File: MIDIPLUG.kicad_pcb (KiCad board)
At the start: 2 copper layers, 34 x 23.4 mm, 28 parts, among them J1 Wavetable Connector, U1 LP2985-3.3, U2 SAM2695, U3 4050, Y1 12Mhz

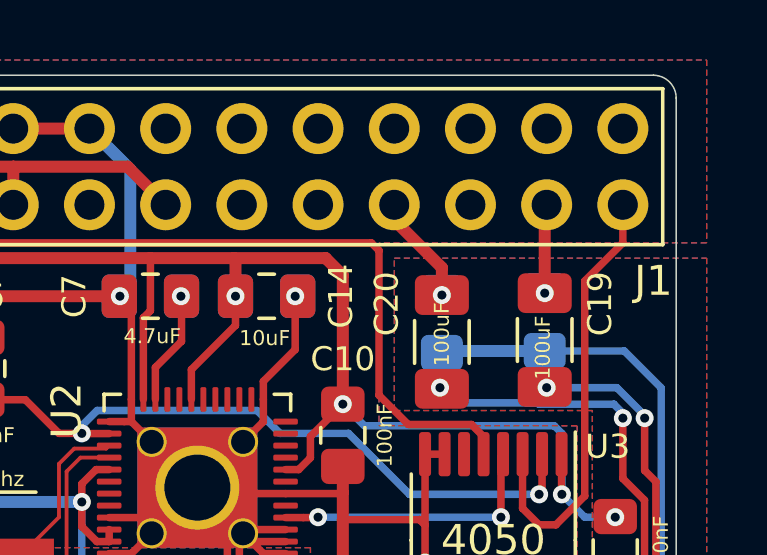
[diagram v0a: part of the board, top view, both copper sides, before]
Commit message: Connect GNDA
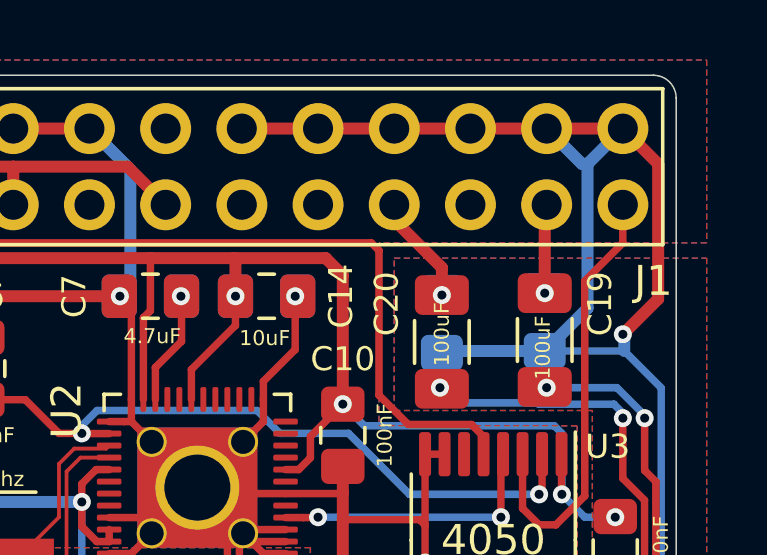
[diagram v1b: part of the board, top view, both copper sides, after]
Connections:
- J1 pad 15: (no net) -> GNDA
- J1 pad 17: (no net) -> GNDA
- J1 pad 19: (no net) -> GNDA
- J1 pad 21: (no net) -> GNDA
- J1 pad 23: (no net) -> GNDA
- J1 pad 25: (no net) -> GNDA
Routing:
- net GNDA: track 47.0 -> 78.4 mm, vias 2 -> 3
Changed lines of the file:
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@@
     (thickness 1.6)
     (drawings 13)
-    (tracks 331)
+    (tracks 348)
     (zones 0)
     (modules 28)
@@
   )
   (setup
-    (last_trace_width 0.127)
+    (last_trace_width 0.4)
     (user_trace_width 0.127)
     (user_trace_width 0.25)
@@
     (add_net "Net-(C6-Pad1)")
     (add_net "Net-(C7-Pad2)")
+    (add_net "Net-(J1-Pad12)")
+    (add_net "Net-(J1-Pad13)")
+    (add_net "Net-(J1-Pad16)")
+    (add_net "Net-(J1-Pad18)")
+    (add_net "Net-(J1-Pad2)")
+    (add_net "Net-(J1-Pad22)")
+    (add_net "Net-(J1-Pad8)")
     (add_net "Net-(U2-Pad16)")
+    (add_net "Net-(U2-Pad24)")
+    (add_net "Net-(U2-Pad26)")
+    (add_net "Net-(U2-Pad27)")
+    (add_net "Net-(U2-Pad28)")
+    (add_net "Net-(U2-Pad29)")
+    (add_net "Net-(U2-Pad3)")
+    (add_net "Net-(U2-Pad30)")
+    (add_net "Net-(U2-Pad32)")
+    (add_net "Net-(U2-Pad33)")
+    (add_net "Net-(U2-Pad42)")
+    (add_net "Net-(U2-Pad7)")
+    (add_net "Net-(U3-Pad10)")
+    (add_net "Net-(U3-Pad12)")
+    (add_net "Net-(U3-Pad15)")
+    (add_net "Net-(U3-Pad6)")
   )
   (net_class POWER ""
@@
     (pad 26 thru_hole oval (at -2.54 30.48 90) (size 1.7 1.7) (drill 1) (layers *.Cu *.Mask)
       (net 18 /~RESET_5V))
-    (pad 25 thru_hole oval (at 0 30.48 90) (size 1.7 1.7) (drill 1) (layers *.Cu *.Mask))
+    (pad 25 thru_hole oval (at 0 30.48 90) (size 1.7 1.7) (drill 1) (layers *.Cu *.Mask)
+      (net 10 GNDA))
     (pad 24 thru_hole oval (at -2.54 27.94 90) (size 1.7 1.7) (drill 1) (layers *.Cu *.Mask)
       (net 16 /AOUT_L))
-    (pad 23 thru_hole oval (at 0 27.94 90) (size 1.7 1.7) (drill 1) (layers *.Cu *.Mask))
+    (pad 23 thru_hole oval (at 0 27.94 90) (size 1.7 1.7) (drill 1) (layers *.Cu *.Mask)
+      (net 10 GNDA))
     (pad 22 thru_hole oval (at -2.54 25.4 90) (size 1.7 1.7) (drill 1) (layers *.Cu *.Mask))
-    (pad 21 thru_hole oval (at 0 25.4 90) (size 1.7 1.7) (drill 1) (layers *.Cu *.Mask))
+    (pad 21 thru_hole oval (at 0 25.4 90) (size 1.7 1.7) (drill 1) (layers *.Cu *.Mask)
+      (net 10 GNDA))
     (pad 20 thru_hole oval (at -2.54 22.86 90) (size 1.7 1.7) (drill 1) (layers *.Cu *.Mask)
       (net 17 /AOUT_R))
-    (pad 19 thru_hole oval (at 0 22.86 90) (size 1.7 1.7) (drill 1) (layers *.Cu *.Mask))
+    (pad 19 thru_hole oval (at 0 22.86 90) (size 1.7 1.7) (drill 1) (layers *.Cu *.Mask)
+      (net 10 GNDA))
     (pad 18 thru_hole oval (at -2.54 20.32 90) (size 1.7 1.7) (drill 1) (layers *.Cu *.Mask))
-    (pad 17 thru_hole oval (at 0 20.32 90) (size 1.7 1.7) (drill 1) (layers *.Cu *.Mask))
+    (pad 17 thru_hole oval (at 0 20.32 90) (size 1.7 1.7) (drill 1) (layers *.Cu *.Mask)
+      (net 10 GNDA))
     (pad 16 thru_hole oval (at -2.54 17.78 90) (size 1.7 1.7) (drill 1) (layers *.Cu *.Mask))
-    (pad 15 thru_hole oval (at 0 17.78 90) (size 1.7 1.7) (drill 1) (layers *.Cu *.Mask))
+    (pad 15 thru_hole oval (at 0 17.78 90) (size 1.7 1.7) (drill 1) (layers *.Cu *.Mask)
+      (net 10 GNDA))
     (pad 14 thru_hole oval (at -2.54 15.24 90) (size 1.7 1.7) (drill 1) (layers *.Cu *.Mask)
       (net 14 VCC))
@@
   (segment (start 126.3015 93.684) (end 124.206 93.684) (width 0.4) (layer B.Cu) (net 10))
   (segment (start 140.217004 93.970996) (end 138.684 95.504) (width 0.25) (layer B.Cu) (net 10))
+  (segment (start 126.238 74.422) (end 128.778 74.422) (width 0.4) (layer F.Cu) (net 10))
+  (segment (start 128.778 74.422) (end 131.318 74.422) (width 0.4) (layer F.Cu) (net 10))
+  (segment (start 131.318 74.422) (end 133.858 74.422) (width 0.4) (layer F.Cu) (net 10))
+  (segment (start 133.858 74.422) (end 136.398 74.422) (width 0.4) (layer F.Cu) (net 10))
+  (segment (start 136.398 74.422) (end 138.938 74.422) (width 0.4) (layer F.Cu) (net 10))
+  (segment (start 137.760999 80.409001) (end 136.3345 81.8355) (width 0.4) (layer B.Cu) (net 10))
+  (segment (start 137.760999 75.599001) (end 137.760999 80.409001) (width 0.4) (layer B.Cu) (net 10))
+  (segment (start 138.938 74.422) (end 137.760999 75.599001) (width 0.4) (layer B.Cu) (net 10))
+  (segment (start 137.575001 75.599001) (end 136.398 74.422) (width 0.4) (layer B.Cu) (net 10))
+  (segment (start 137.760999 75.599001) (end 137.575001 75.599001) (width 0.4) (layer B.Cu) (net 10))
+  (segment (start 140.115001 75.599001) (end 140.115001 80.102999) (width 0.4) (layer F.Cu) (net 10))
+  (segment (start 138.938 74.422) (end 140.115001 75.599001) (width 0.4) (layer F.Cu) (net 10))
+  (segment (start 140.115001 80.102999) (end 138.938 81.28) (width 0.4) (layer F.Cu) (net 10))
+  (segment (start 138.938 81.28) (end 138.938 81.28) (width 0.4) (layer F.Cu) (net 10))
+  (via (at 138.938 81.28) (size 0.6) (drill 0.3) (layers F.Cu B.Cu) (net 10))
+  (segment (start 138.9855 81.3275) (end 138.938 81.28) (width 0.4) (layer B.Cu) (net 10))
+  (segment (start 138.9855 81.8355) (end 138.9855 81.3275) (width 0.4) (layer B.Cu) (net 10))
   (via (at 126.238 91.44) (size 0.6) (drill 0.3) (layers F.Cu B.Cu) (net 11))
   (via (at 124.3075 90.402695) (size 0.6) (drill 0.3) (layers F.Cu B.Cu) (net 11))

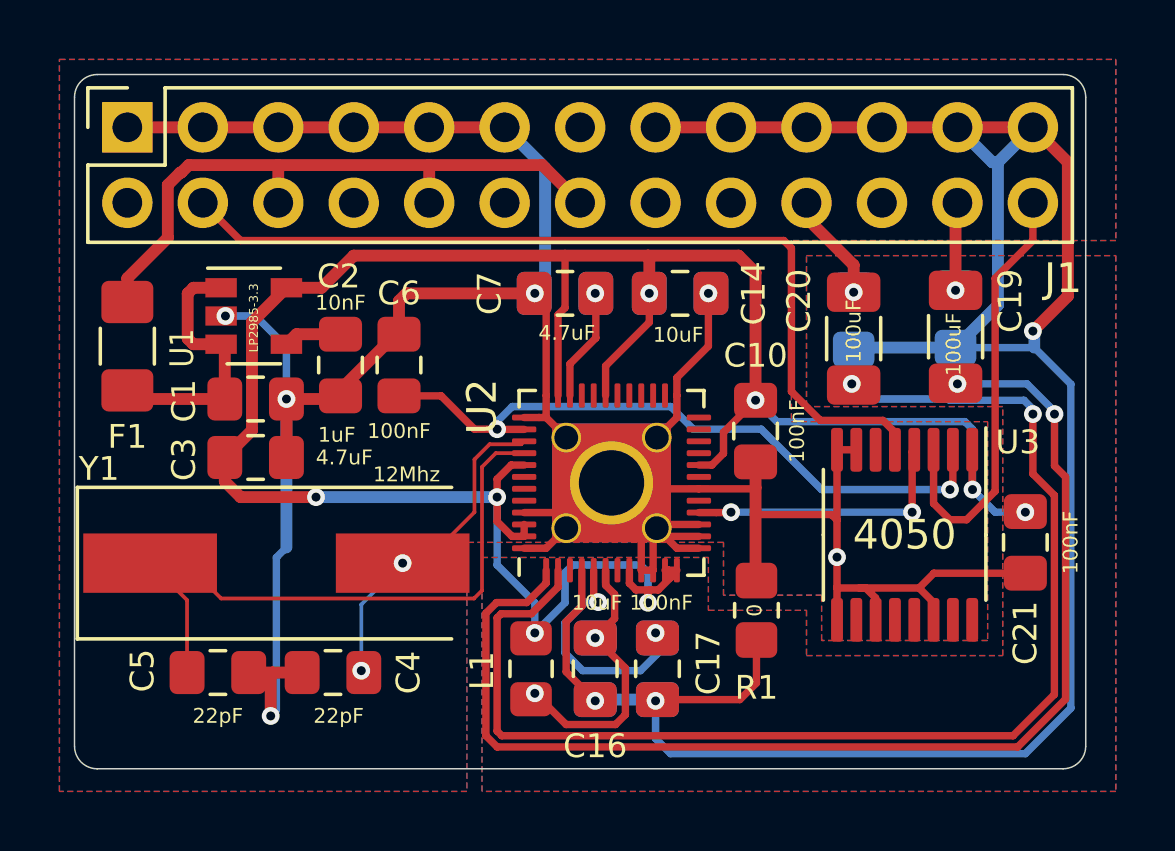
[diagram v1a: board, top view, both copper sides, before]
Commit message: Add missing mask on backside and redo gerbers
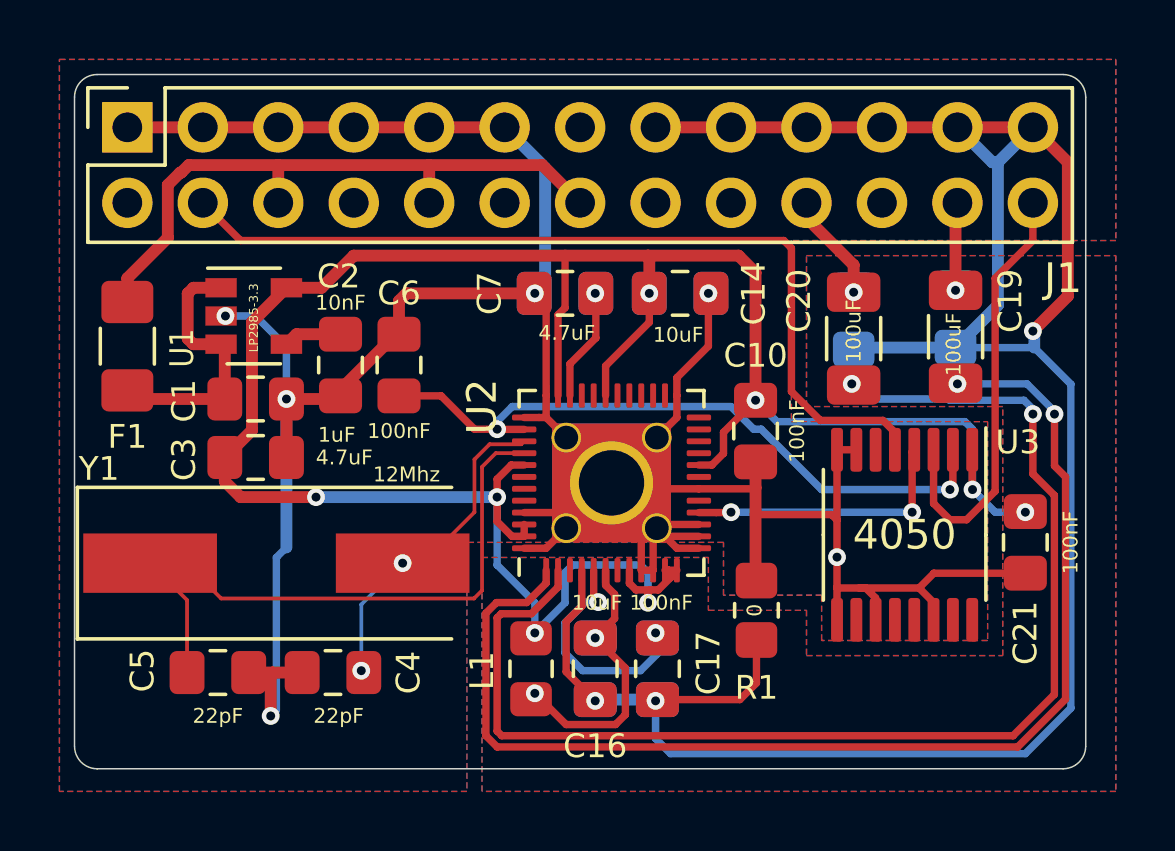
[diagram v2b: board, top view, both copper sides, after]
